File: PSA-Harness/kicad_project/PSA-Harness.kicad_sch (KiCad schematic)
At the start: 15 parts, among them J1 to_EPS_1, J10 B2B_1, J11 B2B_2, J2 to_EPS_2, J3 to_ESP_3, J4 to_car_1, J5 to_car_2, J6 to_car_3, J7 USB_C_Receptacle, J8 B2B_1, J9 B2B_2, K1 G6K-2G-Y DC5

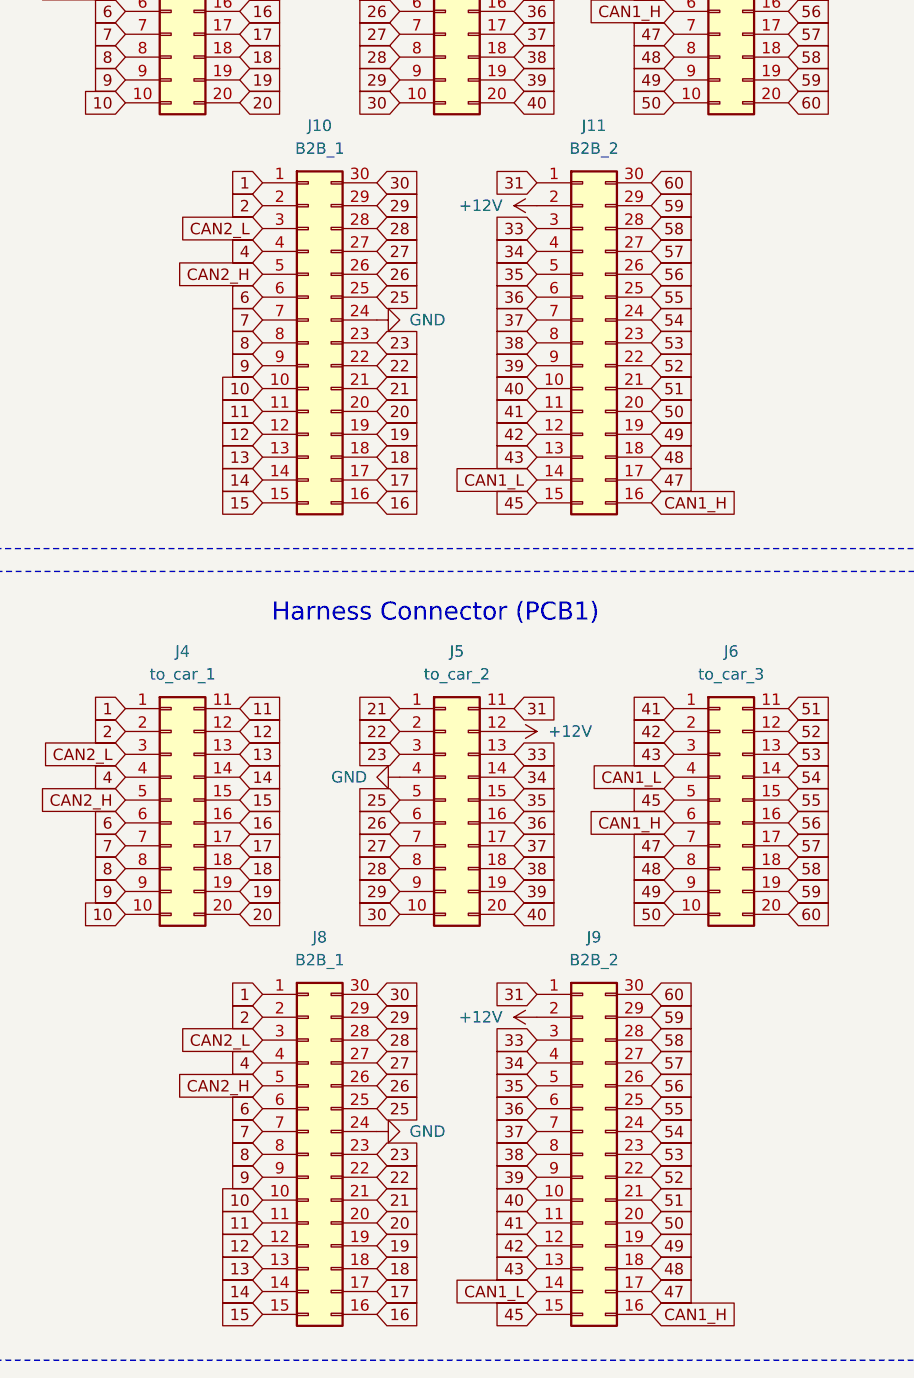
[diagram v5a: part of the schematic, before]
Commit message: chg: rearrange pcb interconnect pins
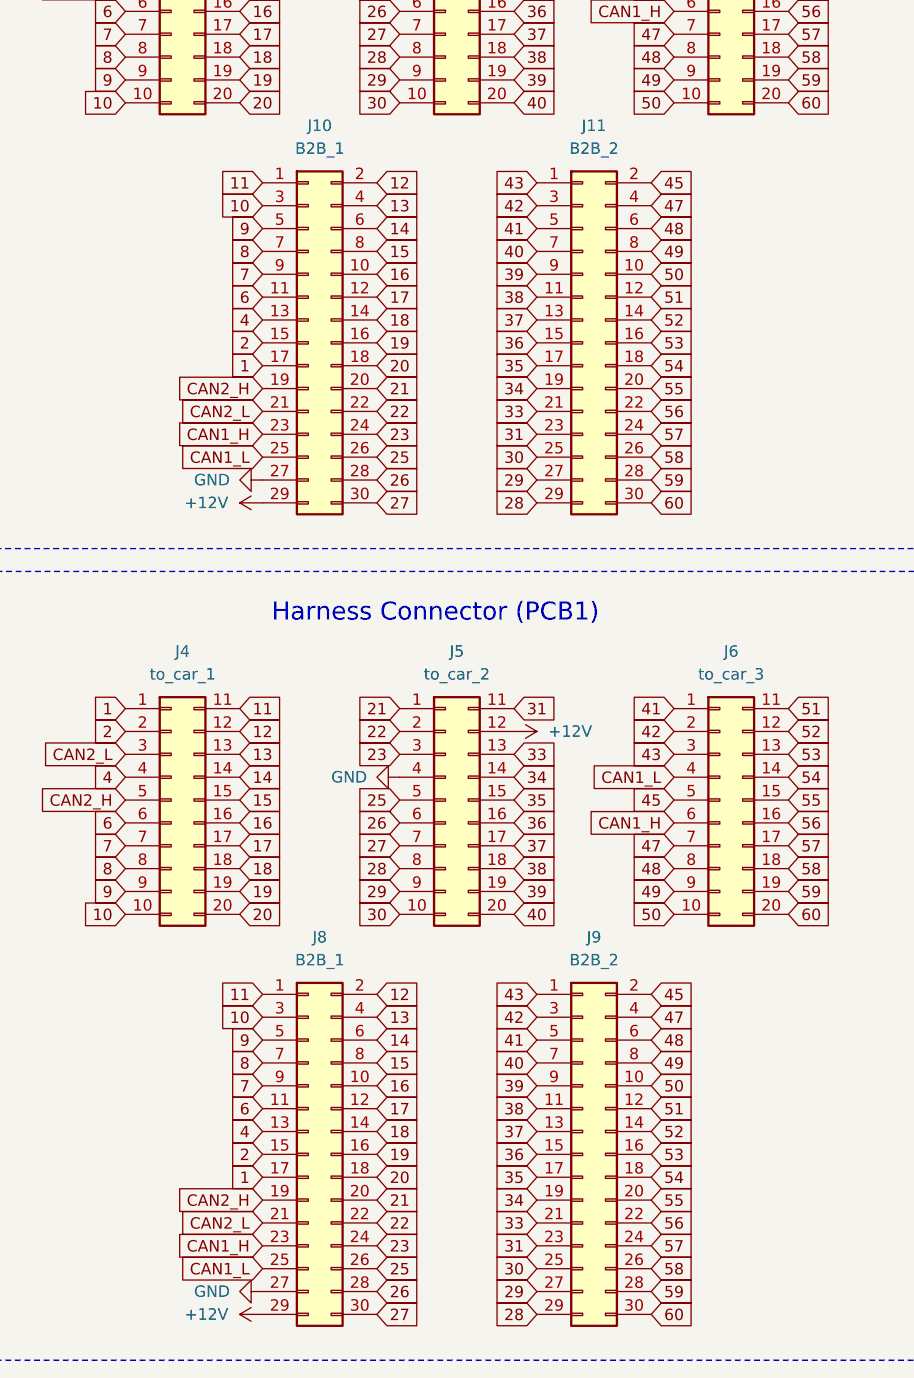
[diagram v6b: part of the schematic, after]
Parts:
- removed J10, J8: B2B_1, Connector_PinHeader_1.27mm:PinHeader_2x15_P1.27mm_Vertical, symbol Connector_Generic:Conn_02x15_Counter_Clockwise
- removed J11, J9: B2B_2, Connector_PinHeader_1.27mm:PinHeader_2x15_P1.27mm_Vertical, symbol Connector_Generic:Conn_02x15_Counter_Clockwise
- added J10, J8: B2B_1, symbol Connector_Generic:Conn_02x15_Odd_Even
- added J11, J9: B2B_2, symbol Connector_Generic:Conn_02x15_Odd_Even
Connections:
- net +12V: now also J10.29 (Pin_29), J8.29 (Pin_29)
- net 1: now also J10.17 (Pin_17), J8.17 (Pin_17)
- net 10: now also J10.3 (Pin_3), J8.3 (Pin_3)
- net 11: now also J10.1 (Pin_1), J8.1 (Pin_1)
- net 12: now also J10.2 (Pin_2), J8.2 (Pin_2)
- net 13: now also J10.4 (Pin_4), J8.4 (Pin_4)
- net 14: now also J10.6 (Pin_6), J8.6 (Pin_6)
- net 15: now also J10.8 (Pin_8), J8.8 (Pin_8)
- net 16: now also J10.10 (Pin_10), J8.10 (Pin_10)
- net 17: now also J10.12 (Pin_12), J8.12 (Pin_12)
- net 18: now also J10.14 (Pin_14), J8.14 (Pin_14)
- net 19: now also J10.16 (Pin_16), J8.16 (Pin_16)
- net 2: now also J10.15 (Pin_15), J8.15 (Pin_15)
- net 20: now also J10.18 (Pin_18), J8.18 (Pin_18)
- net 21: now also J10.20 (Pin_20), J8.20 (Pin_20)
- net 22: now also J10.22 (Pin_22), J8.22 (Pin_22)
- net 23: now also J10.24 (Pin_24), J8.24 (Pin_24)
- net 25: now also J10.26 (Pin_26), J8.26 (Pin_26)
- net 26: now also J10.28 (Pin_28), J8.28 (Pin_28)
- net 27: now also J10.30 (Pin_30), J8.30 (Pin_30)
- net 28: now also J11.29 (Pin_29), J9.29 (Pin_29)
- net 29: now also J11.27 (Pin_27), J9.27 (Pin_27)
- net 30: now also J11.25 (Pin_25), J9.25 (Pin_25)
- net 31: now also J11.23 (Pin_23), J9.23 (Pin_23)
- net 33: now also J11.21 (Pin_21), J9.21 (Pin_21)
- net 34: now also J11.19 (Pin_19), J9.19 (Pin_19)
- net 35: now also J11.17 (Pin_17), J9.17 (Pin_17)
- net 36: now also J11.15 (Pin_15), J9.15 (Pin_15)
- net 37: now also J11.13 (Pin_13), J9.13 (Pin_13)
- net 38: now also J11.11 (Pin_11), J9.11 (Pin_11)
- net 39: now also J11.9 (Pin_9), J9.9 (Pin_9)
- net 4: now also J10.13 (Pin_13), J8.13 (Pin_13)
- net 40: now also J11.7 (Pin_7), J9.7 (Pin_7)
- net 41: now also J11.5 (Pin_5), J9.5 (Pin_5)
- net 42: now also J11.3 (Pin_3), J9.3 (Pin_3)
- net 43: now also J11.1 (Pin_1), J9.1 (Pin_1)
- net 45: now also J11.2 (Pin_2), J9.2 (Pin_2)
- net 47: now also J11.4 (Pin_4), J9.4 (Pin_4)
- net 48: now also J11.6 (Pin_6), J9.6 (Pin_6)
- net 49: now also J11.8 (Pin_8), J9.8 (Pin_8)
- net 50: now also J11.10 (Pin_10), J9.10 (Pin_10)
- net 51: now also J11.12 (Pin_12), J9.12 (Pin_12)
- net 52: now also J11.14 (Pin_14), J9.14 (Pin_14)
- net 53: now also J11.16 (Pin_16), J9.16 (Pin_16)
- net 54: now also J11.18 (Pin_18), J9.18 (Pin_18)
- net 55: now also J11.20 (Pin_20), J9.20 (Pin_20)
- net 56: now also J11.22 (Pin_22), J9.22 (Pin_22)
- net 57: now also J11.24 (Pin_24), J9.24 (Pin_24)
- net 58: now also J11.26 (Pin_26), J9.26 (Pin_26)
- net 59: now also J11.28 (Pin_28), J9.28 (Pin_28)
- net 6: now also J10.11 (Pin_11), J8.11 (Pin_11)
- net 60: now also J11.30 (Pin_30), J9.30 (Pin_30)
- net 7: now also J10.9 (Pin_9), J8.9 (Pin_9)
- net 8: now also J10.7 (Pin_7), J8.7 (Pin_7)
- net 9: now also J10.5 (Pin_5), J8.5 (Pin_5)
- net CAN1_H: now also J10.23 (Pin_23), J8.23 (Pin_23)
- net CAN1_L: now also J10.25 (Pin_25), J8.25 (Pin_25)
- net CAN2_H: now also J10.19 (Pin_19), J8.19 (Pin_19)
- net CAN2_L: now also J10.21 (Pin_21), J8.21 (Pin_21)
- net GND: now also J10.27 (Pin_27), J8.27 (Pin_27)

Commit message: cleared DRC errors
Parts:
- J10, J11, J8, J9: footprint (none) -> Connector_PinHeader_1.27mm:PinHeader_2x15_P1.27mm_Vertical

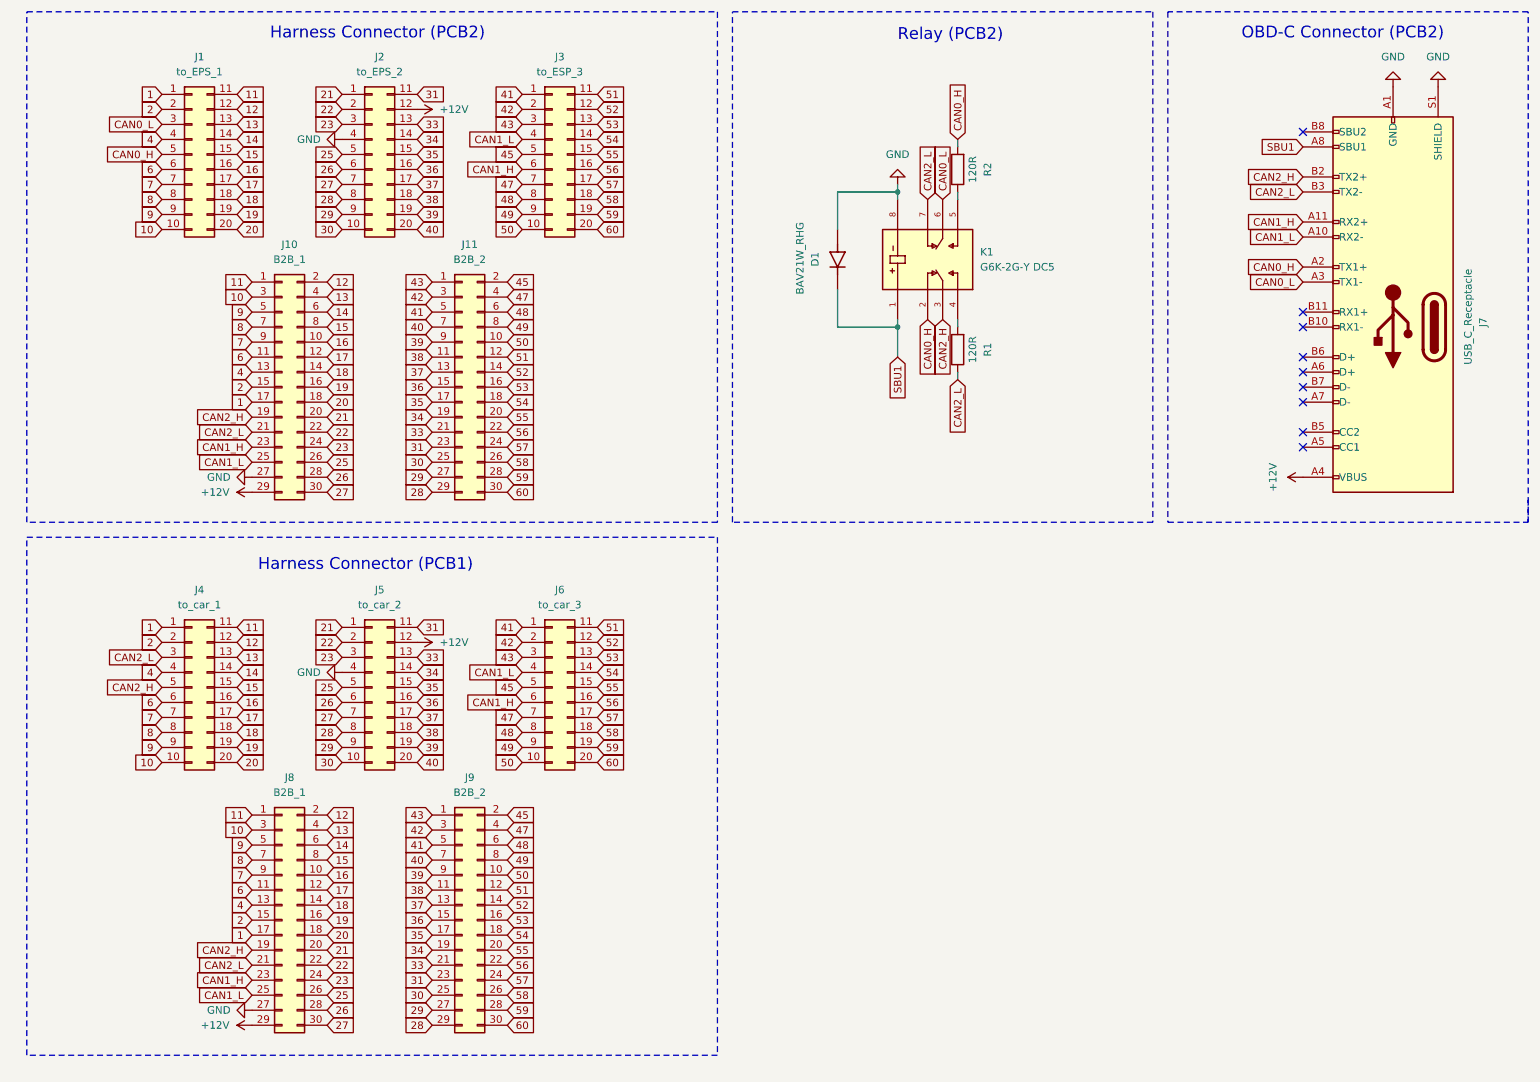
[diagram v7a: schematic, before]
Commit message: chg: schematic: use solid state relay
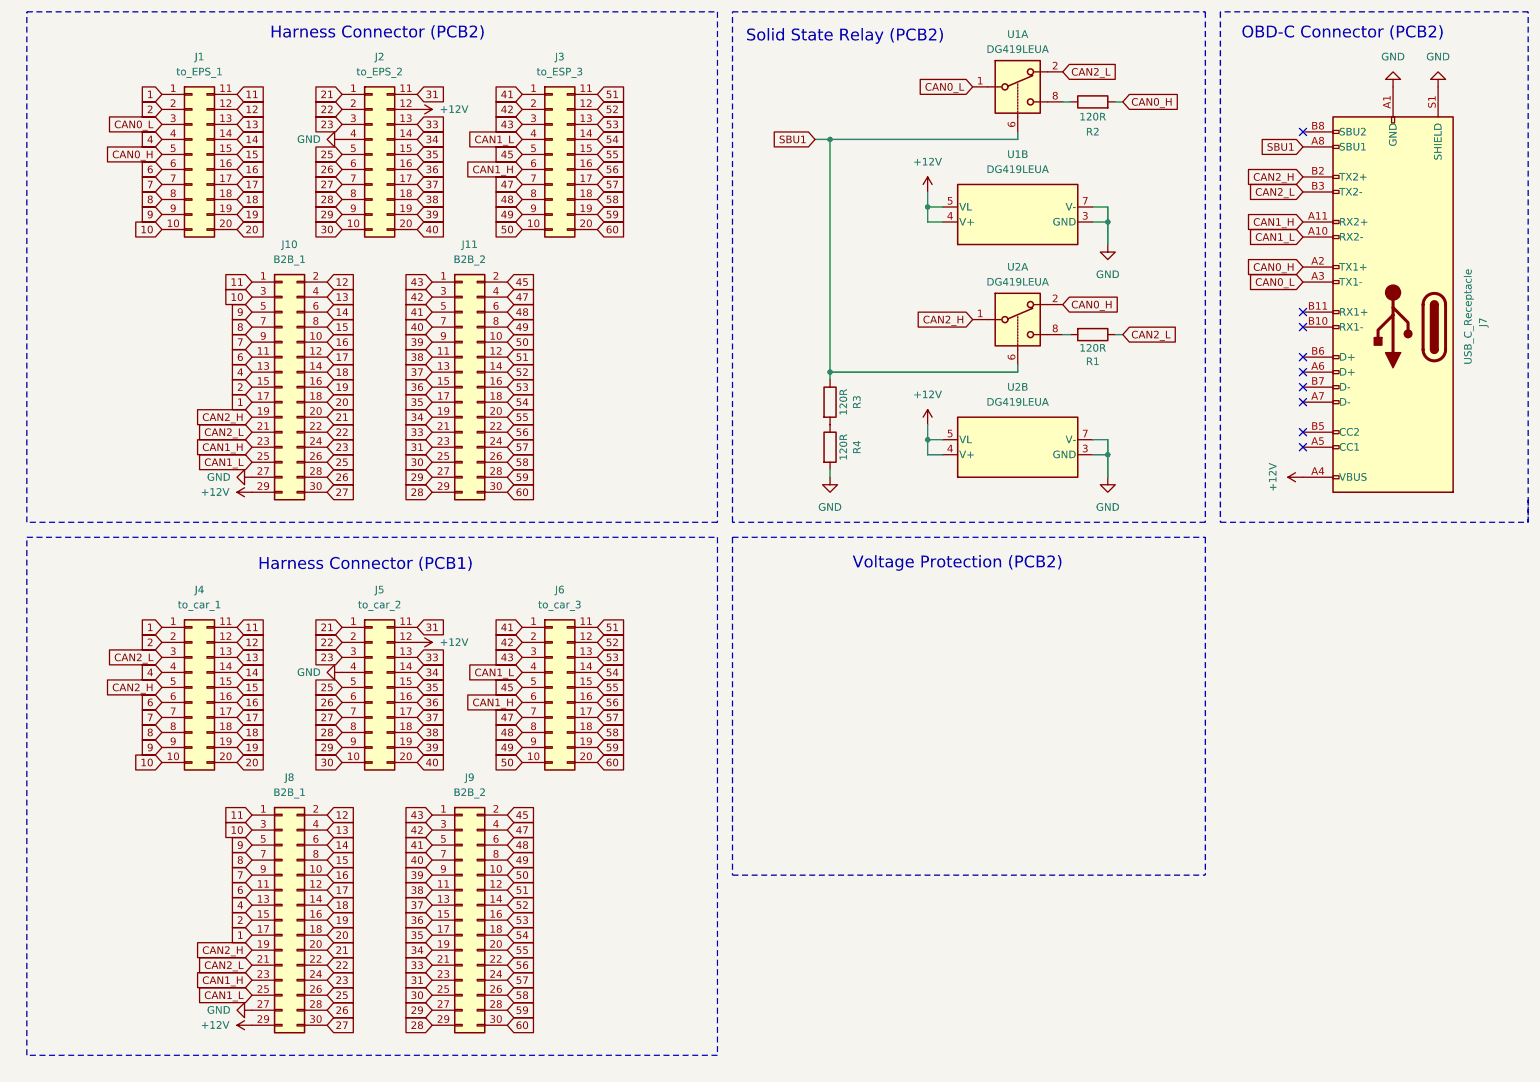
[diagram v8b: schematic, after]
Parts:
- removed D1: BAV21W_RHG, PSA:DIO_BAV21W_RHG, symbol BAV21W_RHG:BAV21W_RHG
- removed K1: G6K-2G-Y DC5, Relay_SMD:Relay_DPDT_Omron_G6K-2G-Y, symbol G6K-2P-Y_DC3:G6K-2P-Y_DC3
- added R3, R4: 120R, Resistor_SMD:R_1206_3216Metric, symbol Device:R
- added U1, U2: DG419LEUA, Package_SO:MSOP-8_3x3mm_P0.65mm, symbol Analog_Switch:DG419LEUA
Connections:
- net +12V: now also U1.4 (V+), U1.5 (VL), U2.4 (V+), U2.5 (VL)
- net CAN0_H: now also U2.2
- net CAN0_L: now also U1.1
- net CAN2_H: now also U2.1
- net CAN2_L: now also U1.2
- net GND: now also R4.2, U1.3 (GND), U1.7 (V-), U2.3 (GND), U2.7 (V-)
- net SBU1: now also R3.1, U1.6, U2.6
- net at R1.2: now also U2.8
- net at R2.1: now also U1.8
- new net: R3.2, R4.1
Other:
- note added: "Solid State Relay (PCB2)"
- note added: "Voltage Protection (PCB2)"
- note removed: "Relay (PCB2)"
- moved on the sheet: R1, R2
